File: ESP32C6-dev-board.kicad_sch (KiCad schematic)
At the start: 7 parts, among them J1 Conn_01x15_Pin, U1 Seeed Studio XIAO SAMD21, U2 AMS1117-3.3

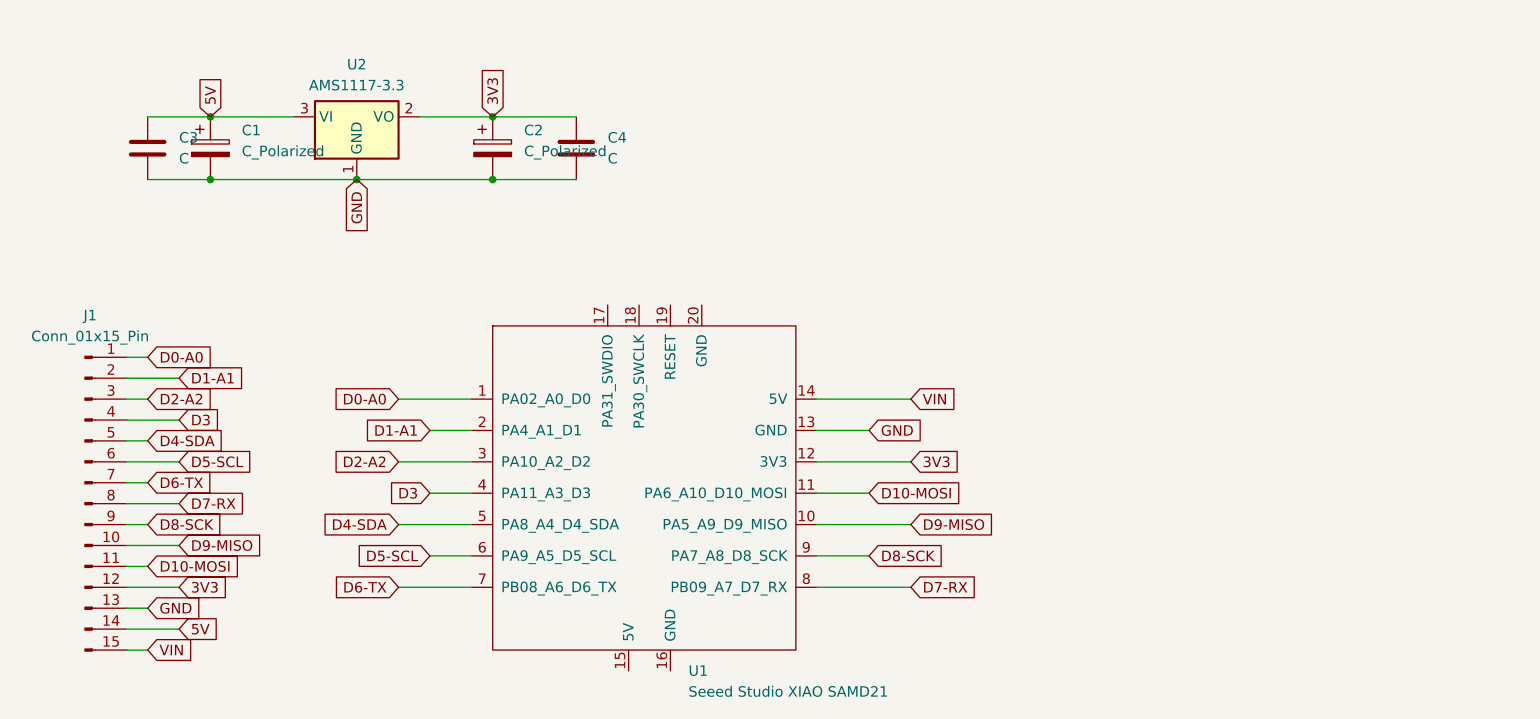
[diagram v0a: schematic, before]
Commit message: Added LM35, DHT11 and WS2812
Added LM35, DHT11 and WS2812
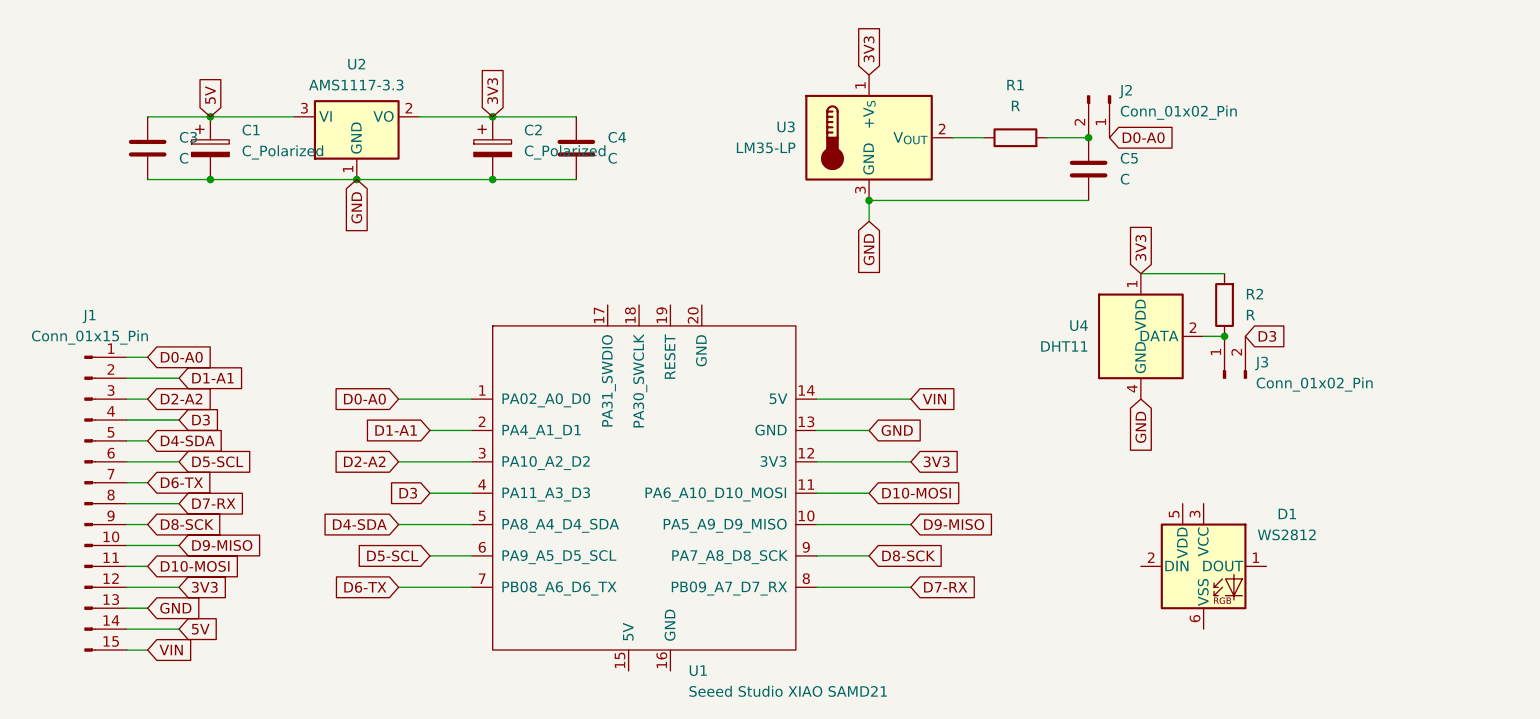
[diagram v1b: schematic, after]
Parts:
- added C5: C, Capacitor_SMD:C_0805_2012Metric, symbol Device:C
- added D1: WS2812, LED_SMD:LED_WS2812_PLCC6_5.0x5.0mm_P1.6mm, symbol LED:WS2812
- added J2, J3: Conn_01x02_Pin, Connector_PinHeader_2.54mm:PinHeader_1x02_P2.54mm_Vertical, symbol Connector:Conn_01x02_Pin
- added R1, R2: R, Resistor_SMD:R_0805_2012Metric, symbol Device:R
- added U3: LM35-LP, Package_TO_SOT_THT:TO-92_Inline, symbol Sensor_Temperature:LM35-LP
- added U4: DHT11, Sensor:Aosong_DHT11_5.5x12.0_P2.54mm, symbol Sensor:DHT11
- J1: footprint Connector_Molex:Molex_SL_171971-0015_1x15_P2.54mm_Vertical -> Connector_PinHeader_2.54mm:PinHeader_1x15_P2.54mm_Vertical
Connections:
- net 3V3: now also R2.2, U3.1 (+V_{S}), U4.1 (VDD)
- net D0-A0: now also J2.1 (Pin_1)
- net D3: now also J3.2 (Pin_2)
- net GND: now also C5.2, U3.3 (GND), U4.4 (GND)
- new net: J3.1 (Pin_1), R2.1, U4.2 (DATA)
- new net: R1.1, U3.2 (V_{OUT})
- new net: C5.1, J2.2 (Pin_2), R1.2

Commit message: Almost finished polising the PCB
Almost finished polising the PCB, minor details are lacking
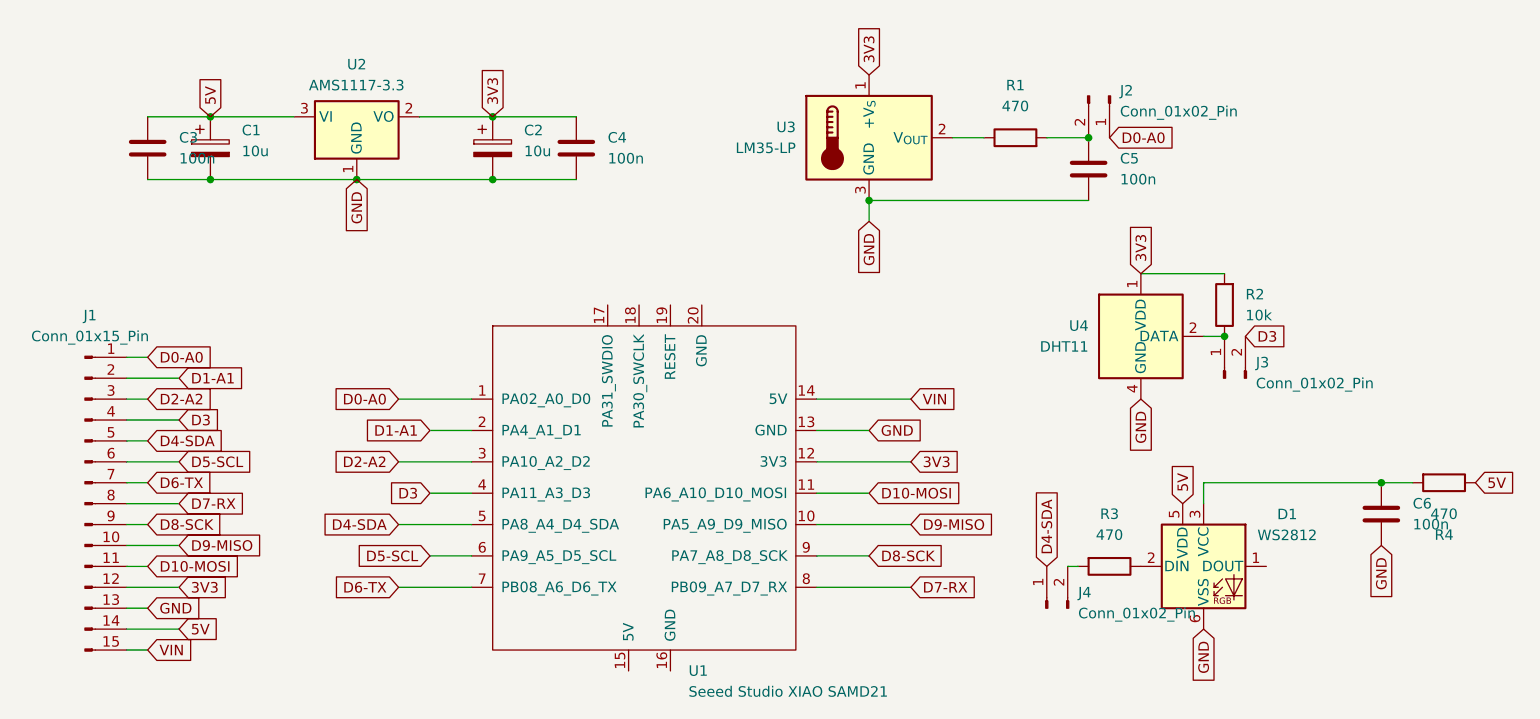
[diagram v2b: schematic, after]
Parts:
- added C6: 100n, Capacitor_SMD:C_0805_2012Metric, symbol Device:C
- added J4: Conn_01x02_Pin, Connector_PinHeader_2.54mm:PinHeader_1x02_P2.54mm_Vertical, symbol Connector:Conn_01x02_Pin
- added R3, R4: 470, Resistor_SMD:R_0805_2012Metric, symbol Device:R
- C1, C2: value C_Polarized -> 10u
- C3, C4, C5: value C -> 100n
- R1: value R -> 470
- R2: value R -> 10k
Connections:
- net 5V: now also D1.5 (VDD), R4.1
- net D4-SDA: now also J4.1 (Pin_1)
- net GND: now also D1.6 (VSS), C6.2
- net at D1.2 (DIN): now also R3.1
- net at D1.3 (VCC): now also C6.1, R4.2
- new net: J4.2 (Pin_2), R3.2
